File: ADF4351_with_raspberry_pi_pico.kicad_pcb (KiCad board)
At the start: 2 copper layers, 62 x 52 mm, 18 parts, among them J1 B4B-XH-A_LF__SN_, J2 302-S101, J3 B4B-XH-A_LF__SN_, J4 Conn_01x03_Socket, J5 Conn_01x05_Socket

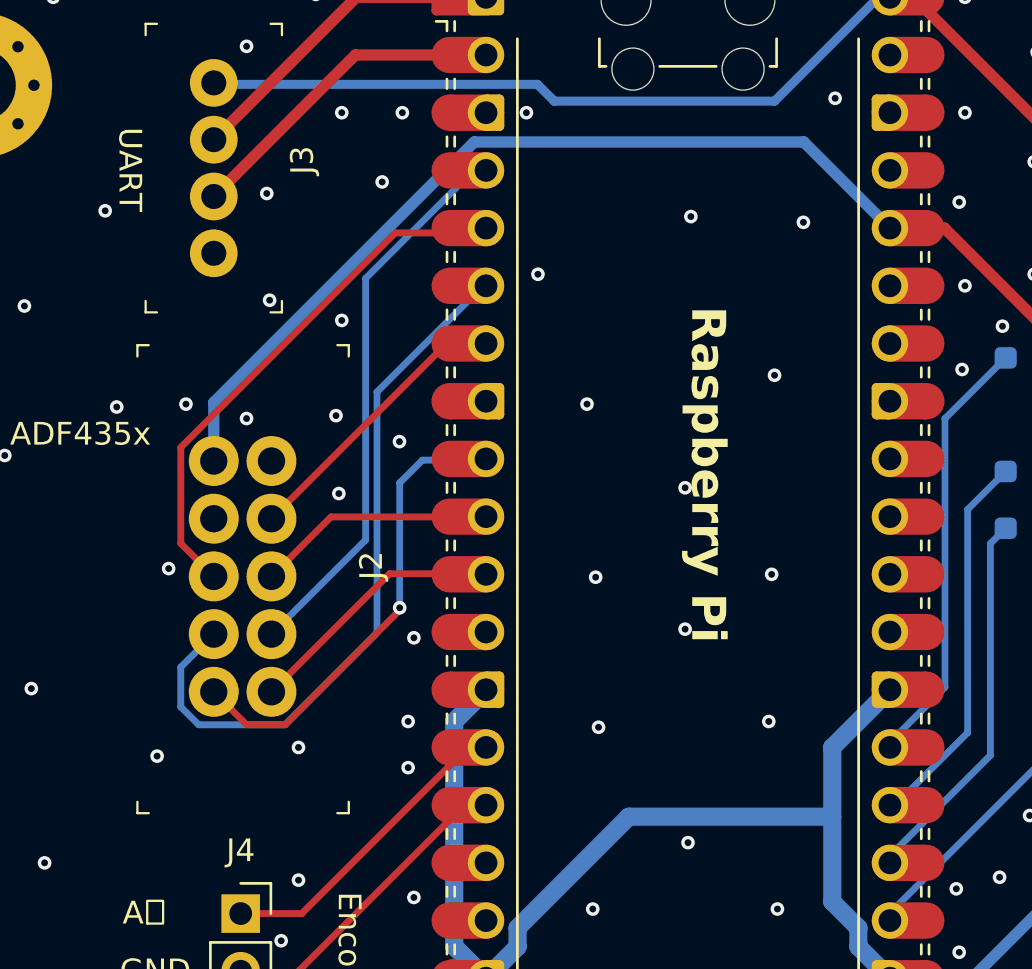
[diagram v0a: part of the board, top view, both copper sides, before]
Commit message: fix 5*2 connector pin
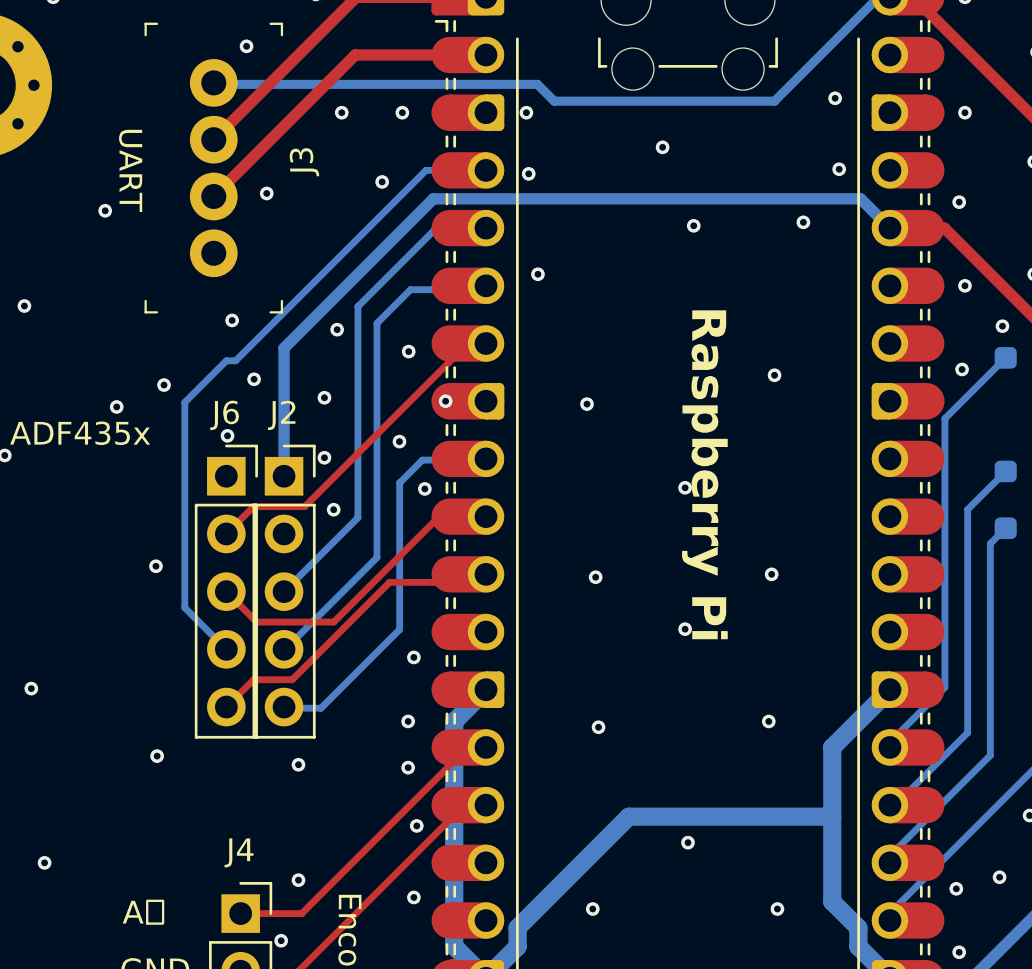
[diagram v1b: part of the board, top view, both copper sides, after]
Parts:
- added J6: Conn_01x05_Pin, Connector_PinSocket_2.54mm:PinSocket_1x05_P2.54mm_Vertical, F.Cu at (102.9, 92.7)
- J2: value 302-S101 -> Conn_01x05_Pin; footprint digikey-footprints:PinHeader_2x5_P2.54mm_Drill1.2mm -> Connector_PinSocket_2.54mm:PinSocket_1x05_P2.54mm_Vertical
- moved J2 0.87 mm to (105.4, 92.7), turned to 0 degrees
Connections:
- J2 pad 1: GND -> +3.3V
- J2 pad 2: +3.3V -> GND
- J2 pad 3: CE -> DAT
- J2 pad 4: GND -> MUX
- J2 pad 5: LE -> PDR
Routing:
- net MUX: track 31.4 -> 21.2 mm
- net CLK: track 24.4 -> 28.9 mm
- net PDR: track 20.9 -> 17.4 mm, vias 1 -> 0
- net CE: track 12.3 -> 15.7 mm
- net LE: track 10.7 -> 13.9 mm
- net +3.3V: track 84.4 -> 81.4 mm
- net DAT: track 23.3 -> 21.0 mm
- net LD: track 11.8 -> 14.1 mm
- net GND: track 48.2 -> 48.0 mm, vias 88 -> 97
